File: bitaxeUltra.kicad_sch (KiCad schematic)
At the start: 16 parts, among them J1 54-00164

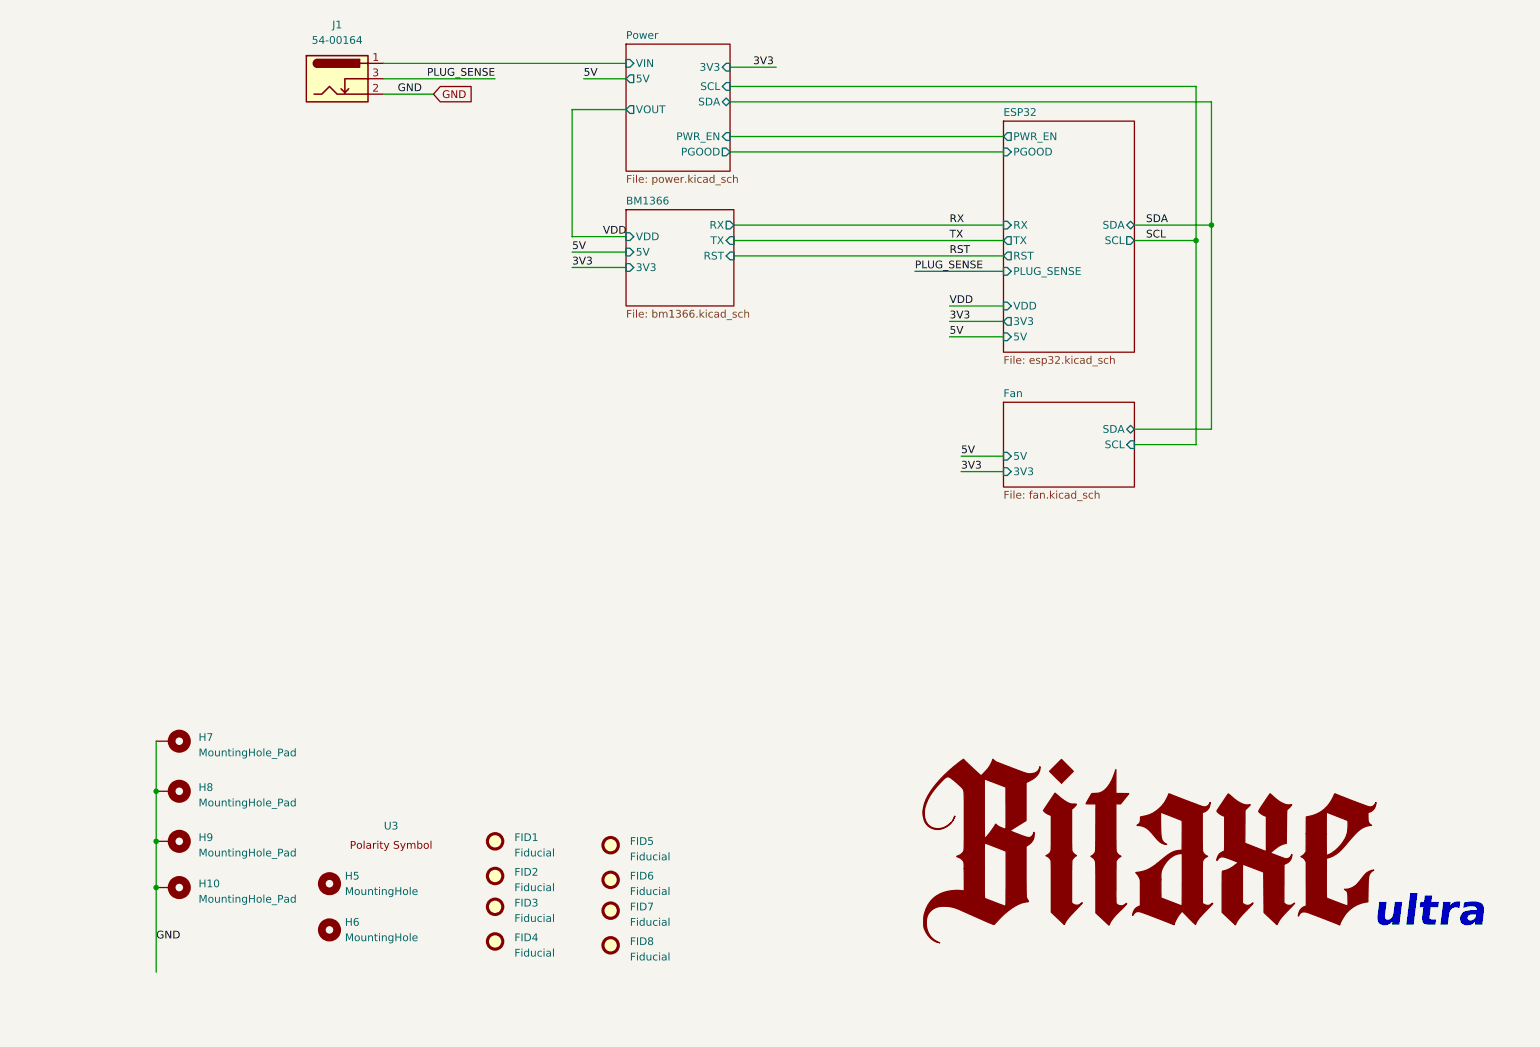
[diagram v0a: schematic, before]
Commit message: Power analysis; updates to 205pd
Started analysis based on the 204 with an architecture diagram and with an smath document. Copied over manually changes from the 205 branch and started updating the schematic with USB PD capabilities. Only added decoy USB PD chip (CH224K), still need to fix power supplies.
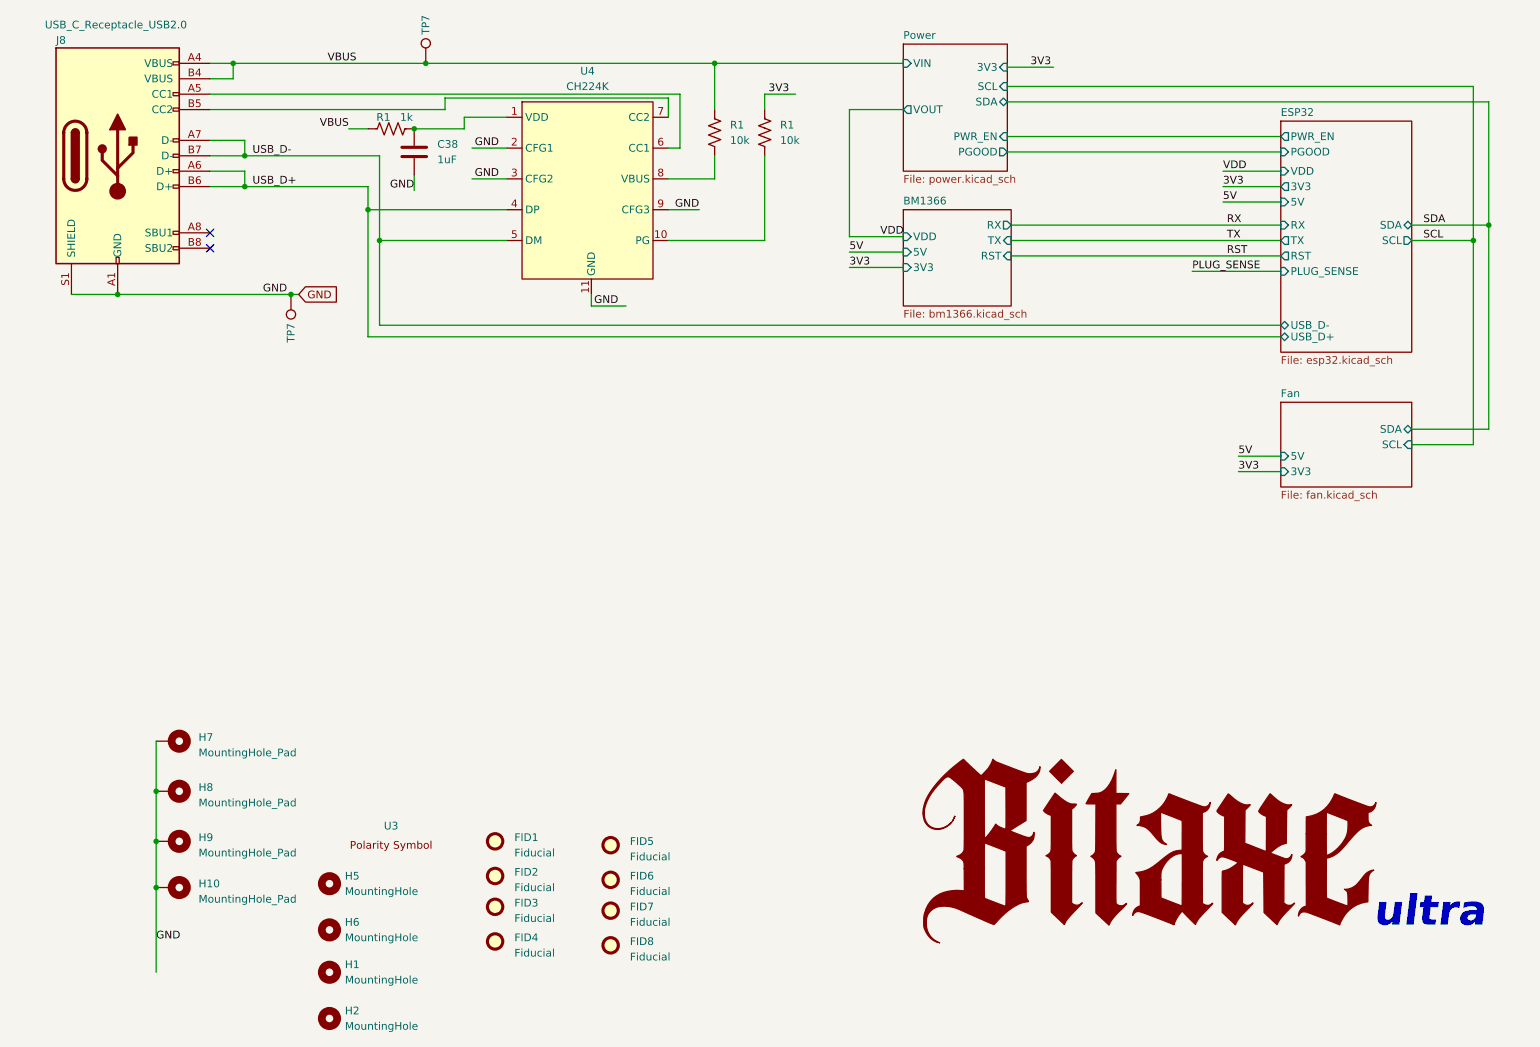
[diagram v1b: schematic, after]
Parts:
- removed J1: 54-00164, bitaxe:BarrelJack_Wuerth_694106106102_2.0x5.5mm, symbol Connector:Barrel_Jack_Switch
- added C38: 1uF, Capacitor_SMD:C_0805_2012Metric, symbol Device:C
- added H1, H2: MountingHole, MountingHole:MountingHole_3.5mm, symbol Mechanical:MountingHole
- added J8: USB_C_Receptacle_USB2.0, Connector_USB:USB_C_Receptacle_GCT_USB4105-xx-A_16P_TopMnt_Horizontal, symbol bitaxe:USB_C_Receptacle_USB2.0
- added R1 (x2): 10k, Resistor_SMD:R_0402_1005Metric, symbol Device:R_US
- added R1: 1k, Resistor_SMD:R_0402_1005Metric, symbol Device:R_US
- added TP7 (x2): TestPoint, TestPoint:TestPoint_Pad_D3.0mm, symbol Connector:TestPoint
- added U4: CH224K, IC:ESSOP-10, symbol bitaxe:CH224K
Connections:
- net 3V3: now also R1.1
- net GND: now also C38.2, J8.A1 (GND), J8.B1 (GND), J8.S1 (SHIELD), TP7.1, U4.11 (GND), U4.2 (CFG1), U4.3 (CFG2), U4.9 (CFG3)
- new net: R1.2, U4.8 (VBUS)
- new net: J8.A5 (CC1), U4.6 (CC1)
- new net: J8.B5 (CC2), U4.7 (CC2)
- new net: C38.1, R1.2, U4.1 (VDD)
- new net: R1.2, U4.10 (PG)
- new net USB_D+: J8.A6 (D+), J8.B6 (D+), U4.4 (DP)
- new net USB_D-: J8.A7 (D-), J8.B7 (D-), U4.5 (DM)
- new net VBUS: J8.A4 (VBUS), J8.B4 (VBUS), R1.1, R1.1, TP7.1
- no-connect marks 0 -> 2
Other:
- sheet ESP32 ports: added USB_D+, USB_D-; removed none
- sheet Power ports: added none; removed 5V

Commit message: Worked on VDD
Started importing SiC431A for VDD supply. Yet to do Vfb, Mode, Pgood, boot, phase, en. Moved power supplies to power page. Configured CH224K to 12V
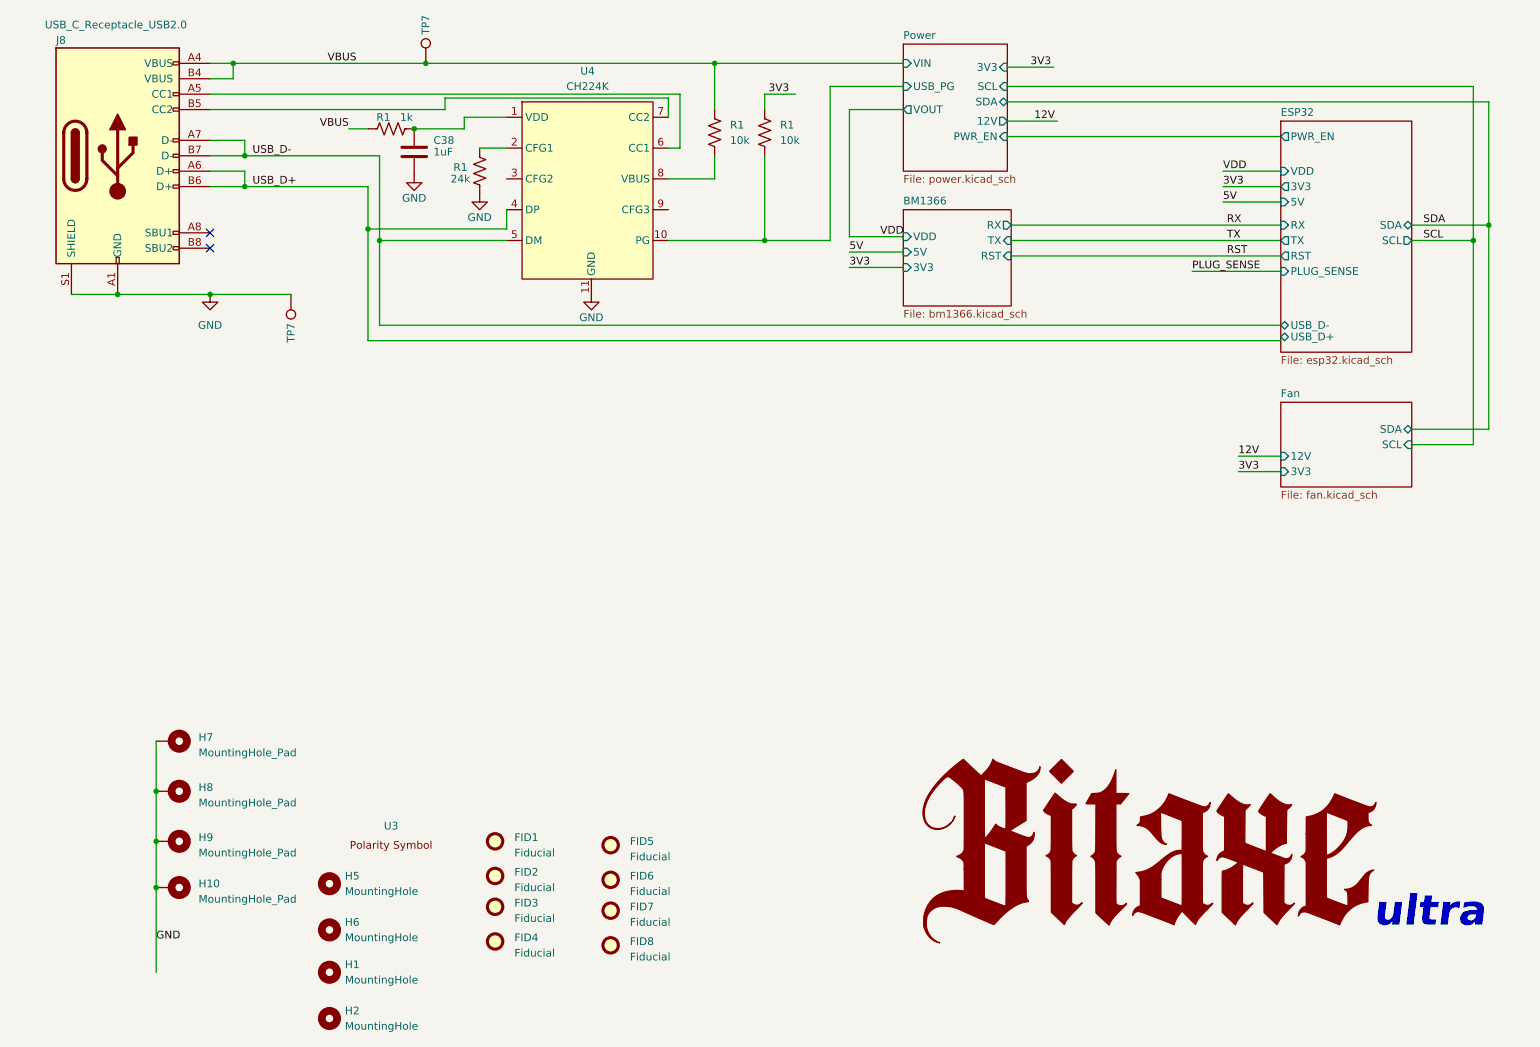
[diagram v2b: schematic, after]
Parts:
- added R1: 24k, Resistor_SMD:R_0402_1005Metric, symbol Device:R_US
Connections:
- net GND: now also R1.1; no longer U4.2 (CFG1), U4.3 (CFG2), U4.9 (CFG3)
- net Power/USB_PG: now reaches R1.2, U4.10 (PG)
- new net: R1.2, U4.2 (CFG1)
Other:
- sheet ESP32 ports: added none; removed PGOOD
- sheet Fan ports: added 12V; removed 5V
- sheet Power ports: added 12V, USB_PG; removed PGOOD

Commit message: SCH Draft 3, PCB Start
Finished some last minute changes to change 1V8 to 1V2 based on discord feedback. Updated level shifter and moved 25MHz oscillator to use 3V3 and be shifted down. Started working on layout.
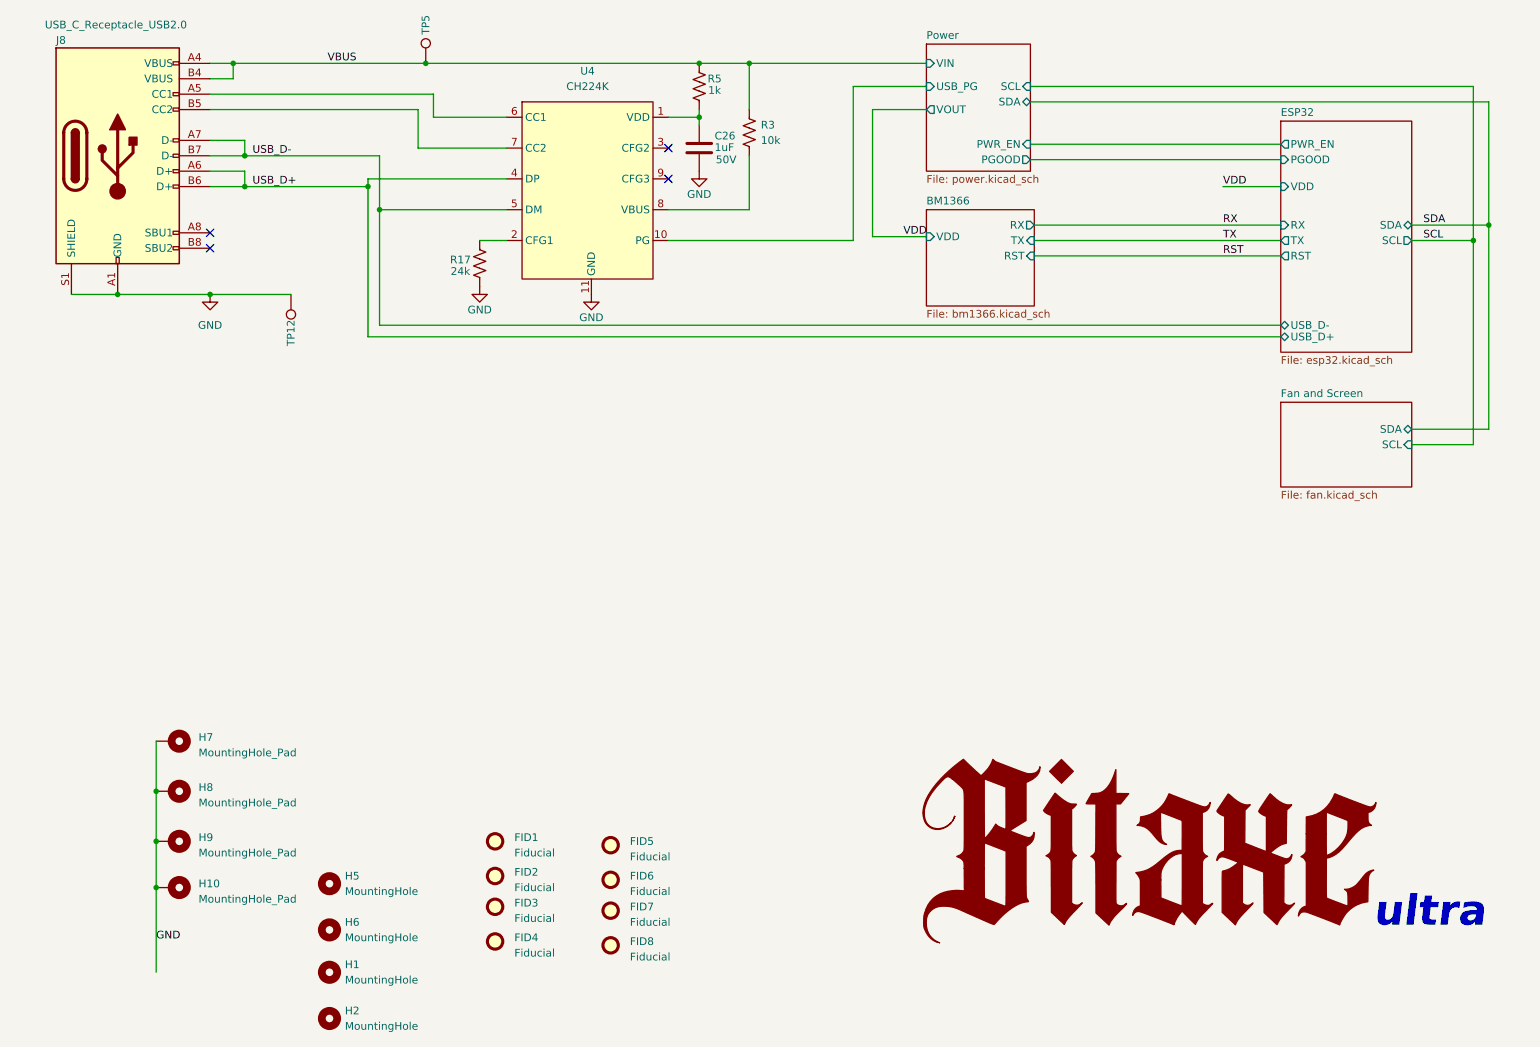
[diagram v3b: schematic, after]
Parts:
- removed C38: 1uF, Capacitor_SMD:C_0805_2012Metric, symbol Device:C
- removed R1: 24k, Resistor_SMD:R_0402_1005Metric, symbol Device:R_US
- removed R1: 1k, Resistor_SMD:R_0402_1005Metric, symbol Device:R_US
- removed R1: 10k, Resistor_SMD:R_0402_1005Metric, symbol Device:R_US
- removed U3: ~, bitaxe:polarity, symbol bitaxe:polarity
- added C26: 1uF, Capacitor_SMD:C_0603_1608Metric, symbol Device:C
- added R17: 24k, Resistor_SMD:R_0402_1005Metric, symbol Device:R_US
- added R5: 1k, Resistor_SMD:R_0402_1005Metric, symbol Device:R_US
- renumbered R1 to R3, TP7 to TP12, TP7 to TP5
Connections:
- net GND: now also C26.2, R17.1
- net VBUS: now also R5.2
- net at U4.2 (CFG1): now also R17.2
- net at U4.1 (VDD): now also C26.1, R5.1
- no-connect marks 2 -> 4
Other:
- sheet Fan renamed Fan and Screen
- sheet BM1366 ports: added none; removed 3V3, 5V
- sheet ESP32 ports: added PGOOD; removed 3V3, 5V, PLUG_SENSE
- sheet Fan and Screen ports: added none; removed 12V, 3V3
- sheet Power ports: added PGOOD; removed 12V, 3V3
- moved on the sheet: R3
